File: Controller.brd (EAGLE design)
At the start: 125 x 65 mm, 70 parts, among them J1 282834-4, J2 282834-2, J3 825457-3, SW1 MULTICOLOR_BUTTON, SW2 MULTICOLOR_BUTTON, SW3 MULTICOLOR_BUTTON, SW4 MULTICOLOR_BUTTON, SW5 MULTICOLOR_BUTTON, SW6 MULTICOLOR_BUTTON, SW7 MULTICOLOR_BUTTON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

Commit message: Added Gerbers
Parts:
- moved R15 0.51 mm to (47.7, 58.2)
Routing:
- net +5V: track 119.9 -> 191.9 mm, vias 14 -> 12
- net VCC: track 43.4 -> 50.9 mm, vias 0 -> 1

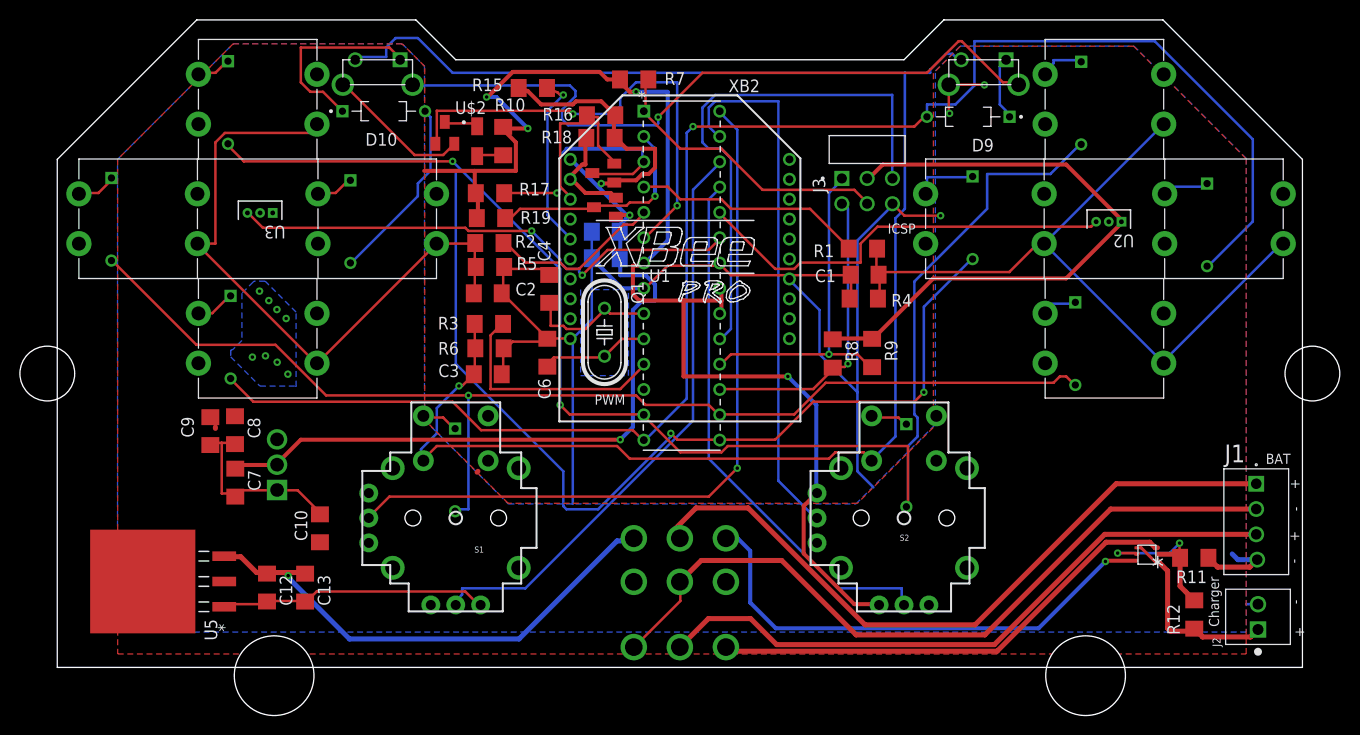
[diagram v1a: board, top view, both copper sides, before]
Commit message: Added Sam's holes
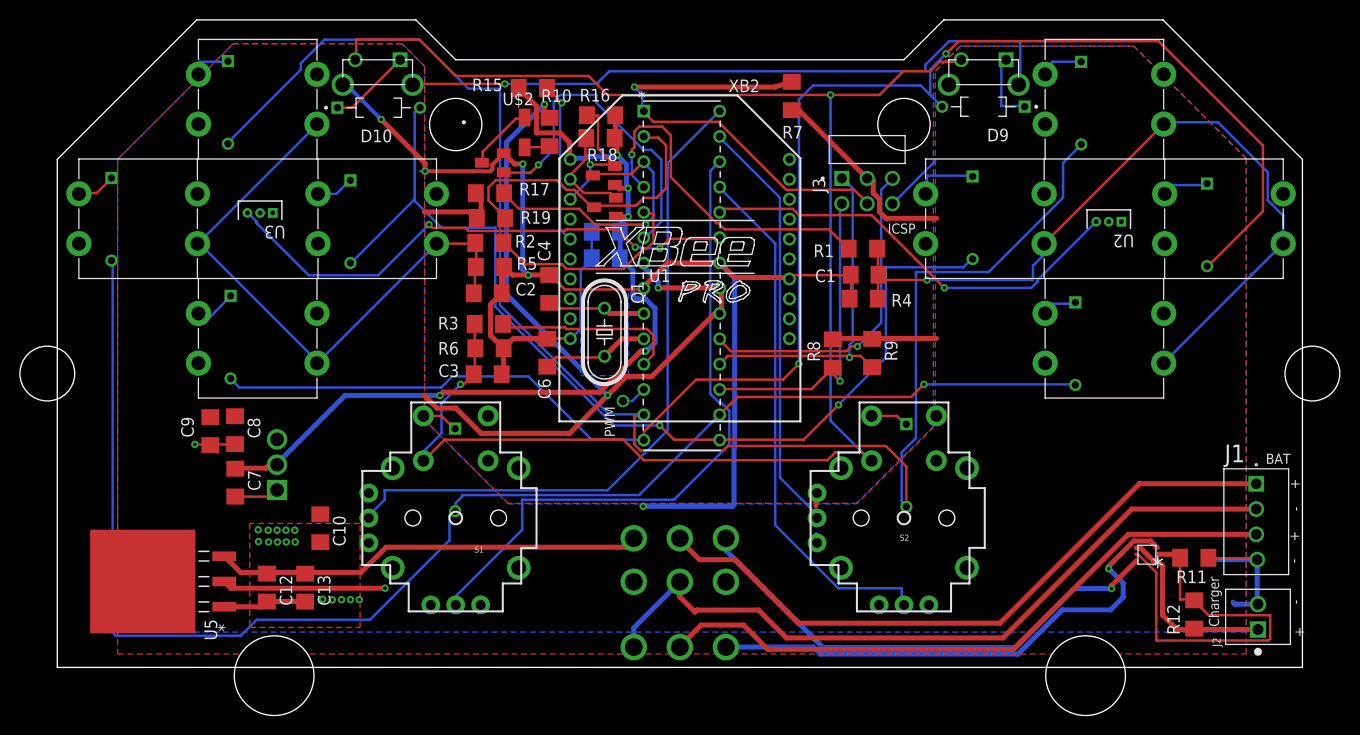
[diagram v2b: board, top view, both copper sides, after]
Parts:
- moved R7 15.9 mm to (73.7, 57.4), turned to 90 degrees
- moved U$3 5.68 mm to (43.7, 50.7), turned to 90 degrees
- moved U$2 4.84 mm to (46.9, 53.7)
- moved R10 4.75 mm to (49.4, 53.8)
- moved D9 1.83 mm to (93.0, 56.3)
- moved D10 0.61 mm to (32.3, 56.2)
- moved U$5 0.25 mm to (54.9, 49.4)
- turned C10 to 270 degrees
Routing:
- net +5V: track 191.9 -> 142.1 mm, vias 12 -> 4
- net R3: track 118.0 -> 146.7 mm
- net N$19: track 17.8 -> 39.8 mm, vias 2 -> 0
- net CLK: track 53.6 -> 32.9 mm, vias 0 -> 1
- net R4: track 143.4 -> 159.7 mm, vias 2 -> 0
- net RESET: track 29.8 -> 45.1 mm, vias 0 -> 1
- net R2: track 116.8 -> 102.2 mm
- net N$6: track 46.5 -> 33.8 mm, vias 2 -> 1
- net +3V3: track 104.0 -> 91.6 mm, vias 3 -> 5
- net C1: track 23.2 -> 35.5 mm, vias 0 -> 1
- net X_RIGHT: track 54.2 -> 42.3 mm
- net N$26: track 19.4 -> 8.28 mm
- net RX: track 22.4 -> 30.8 mm, vias 1 -> 0
- net VCC: track 50.9 -> 43.4 mm, vias 1 -> 0
- net X_LEFT: track 75.6 -> 68.6 mm, vias 1 -> 0
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- added copper zone on layer 1, net GND
- removed copper zone on layer 16, net +5V

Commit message: Read Desc.
* Moved Bumpers 3mm lower
* changed TO diodes to SMD
* Chnaged BOM to shorter actuator buttons
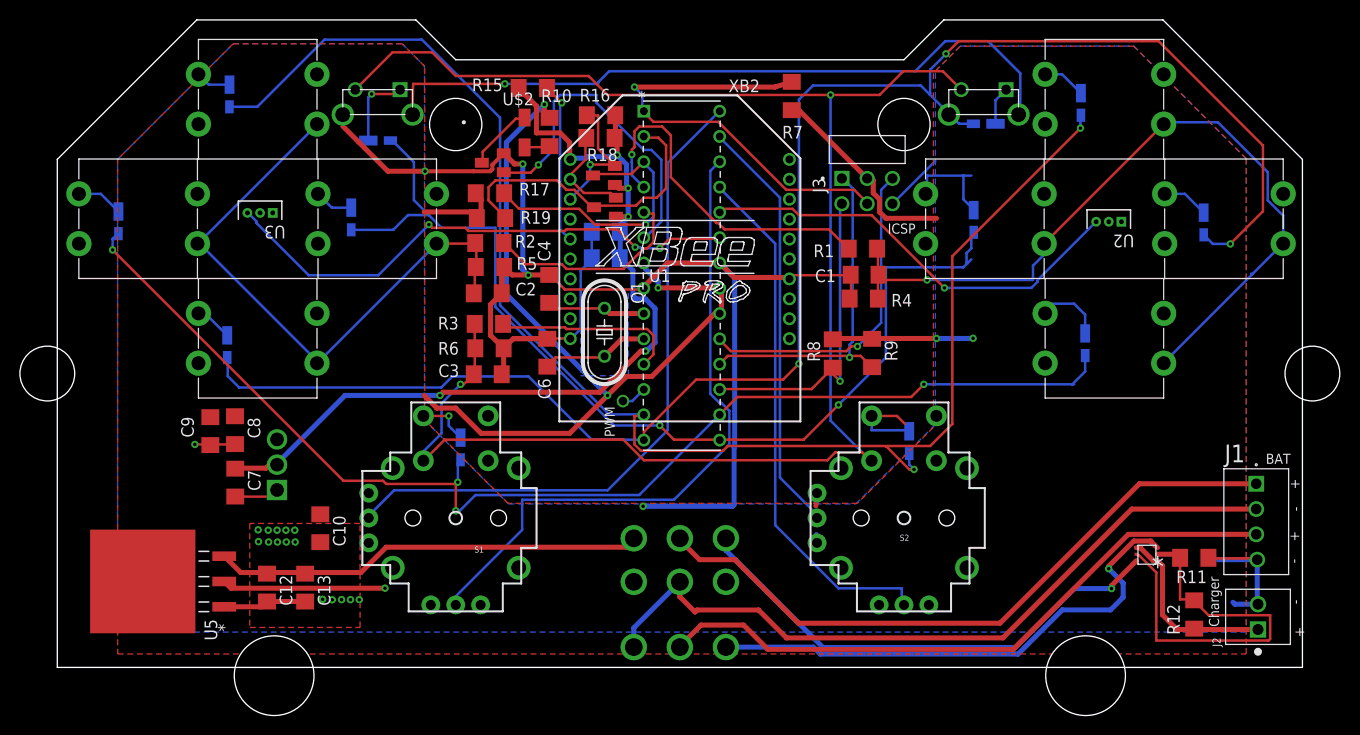
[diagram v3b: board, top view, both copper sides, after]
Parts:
- removed D1, D10, D11, D12, D2, D3, D4, D5, D6, D7, D8, D9: 1N4148, 1N4148:DIOAD829W49L456D191
- added CR1, CR10, CR11, CR12, CR2, CR3, CR4, CR5, CR6, CR7, CR8, CR9: MSS1P6-M3/89ADIODE_MSP3V3-M, Controller:DIODE_MSP3V3-M
- moved U$4 3.00 mm to (93.0, 58.0)
- moved U$6 3.00 mm to (32.2, 58.0)
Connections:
- net N$16: now also CR3.1; no longer D3.C
- net N$18: now also CR2.1; no longer D2.C
- net N$2: now also CR4.1; no longer D4.C
- net N$20: now also CR1.1; no longer D1.C
- net N$21: now also CR7.1; no longer D6.C
- net N$22: now also CR6.1; no longer D7.C
- net N$23: now also CR5.1; no longer D8.C
- net N$24: now also CR12.1; no longer D9.C
- net N$25: now also CR8.1; no longer D5.C
- net N$26: now also CR11.1; no longer D10.C
- net N$27: now also CR10.1; no longer D11.C
- net N$28: now also CR9.1; no longer D12.C
- net R1: now also CR1.2, CR12.2, CR8.2; no longer D1.A, D5.A, D9.A
- net R2: now also CR11.2, CR2.2, CR7.2; no longer D10.A, D2.A, D6.A
- net R3: now also CR10.2, CR3.2, CR6.2; no longer D11.A, D3.A, D7.A
- net R4: now also CR4.2, CR5.2, CR9.2; no longer D12.A, D4.A, D8.A
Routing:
- net R3: track 146.7 -> 122.4 mm, vias 1 -> 4
- net R4: track 159.7 -> 150.0 mm, vias 0 -> 2
- net R1: track 162.5 -> 168.9 mm, vias 2 -> 3
- net N$28: track 3.82 -> 8.92 mm
- net N$18: track 6.51 -> 10.2 mm
- net N$5: track 67.7 -> 71.5 mm
- net +5V: track 142.1 -> 145.9 mm, vias 4 -> 6
- net N$24: track 7.21 -> 3.86 mm
- net N$16: track 4.04 -> 7.31 mm
- net N$27: track 3.71 -> 5.25 mm, vias 0 -> 1
- net GND: track 205.1 -> 204.0 mm, vias 21 -> 20
- net N$22: track 3.96 -> 4.70 mm
- net N$C3: track 168.5 -> 167.9 mm
- net X_LEFT: track 68.6 -> 68.0 mm
- net N$25: track 4.32 -> 3.81 mm
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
